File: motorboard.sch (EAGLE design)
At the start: 21 parts, among them U1 STM32F302_303C2

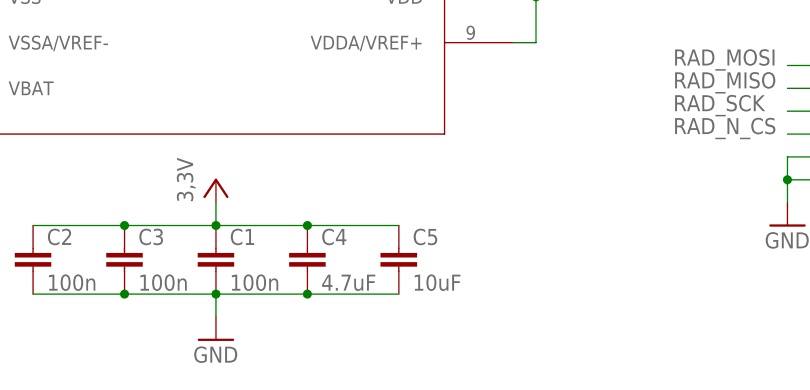
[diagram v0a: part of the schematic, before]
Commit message: fixed capacitors values
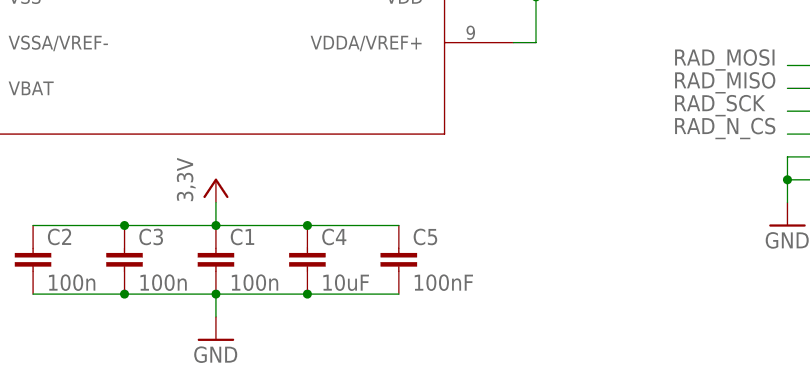
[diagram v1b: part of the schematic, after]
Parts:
- C4: value 4.7uF -> 10uF
- C5: value 10uF -> 100nF
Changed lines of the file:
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@@
 <part name="GND7" library="supply1" deviceset="GND" device=""/>
 <part name="C1" library="resistor" deviceset="C-EU" device="C0805" value="100n"/>
-<part name="C4" library="resistor" deviceset="C-EU" device="C0805" value="4.7uF"/>
-<part name="C5" library="resistor" deviceset="C-EU" device="C0805" value="10uF"/>
+<part name="C4" library="resistor" deviceset="C-EU" device="C0805" value="10uF"/>
+<part name="C5" library="resistor" deviceset="C-EU" device="C0805" value="100nF"/>
 <part name="C6" library="resistor" deviceset="C-EU" device="C0805" value="100n"/>
 <part name="GND8" library="supply1" deviceset="GND" device=""/>
